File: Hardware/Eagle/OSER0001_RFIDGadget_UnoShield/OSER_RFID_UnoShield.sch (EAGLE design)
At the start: 6 parts, among them U1 ARDUINOR3-BPLACE

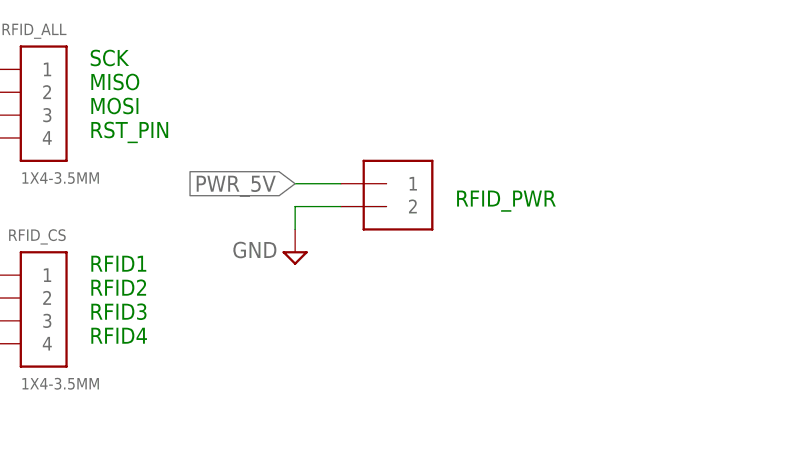
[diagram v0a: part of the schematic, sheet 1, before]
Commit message: 1x3 header pin to allow user select 3V or 5V to RFID reader
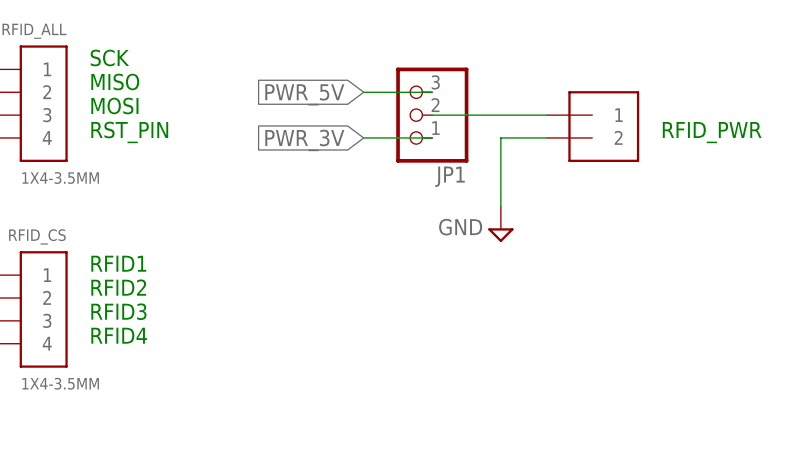
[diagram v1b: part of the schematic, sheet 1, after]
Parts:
- added JP1: (no value), adafruit:PINHD-1X3
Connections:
- new net N$1: JP1.2, RFID_PWR.1
- net PWR_3V: now also JP1.1
- net PWR_5V: now also JP1.3; no longer RFID_PWR.1
